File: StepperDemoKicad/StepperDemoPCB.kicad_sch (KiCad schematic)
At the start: 38 parts, among them J1 Conn_01x05_Male, J2 Conn_01x01_Male, J3 Screw_Terminal_01x03, J4 Screw_Terminal_01x04, J5 Screw_Terminal_01x04, J6 Conn_01x06_Male, M1 Stepper_Motor_bipolar, SW1 SW_DIP_x01, U1 L297, U2 L298N

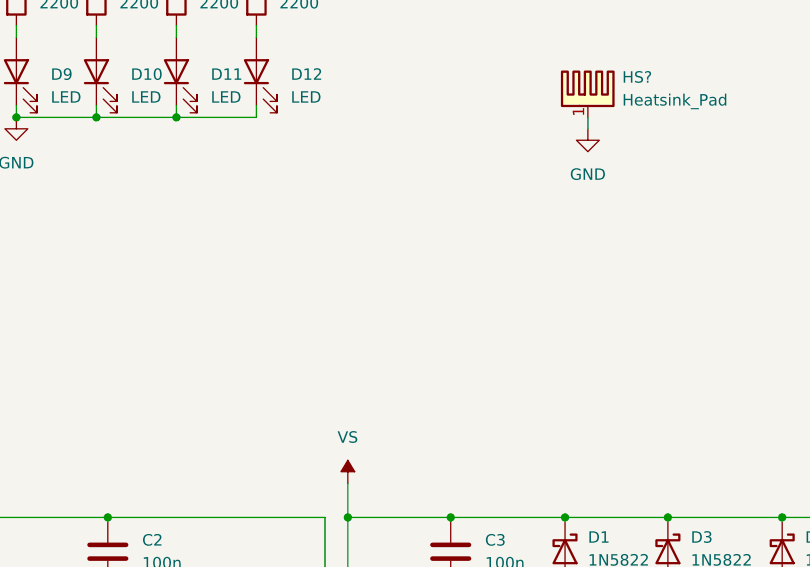
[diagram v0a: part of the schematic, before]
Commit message: smd Diode
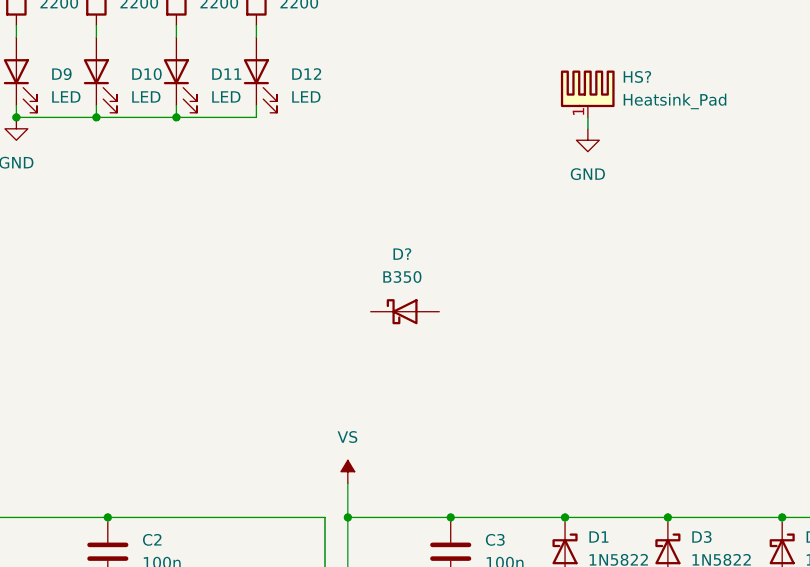
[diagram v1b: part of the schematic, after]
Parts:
- added D?: B350, Diode_SMD:D_SMC, symbol Diode:B350
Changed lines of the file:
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@@
+    (pin "2")
+  )
+  (symbol (lib_id "Diode:B350") (at 156.21 60.96 0) (unit 1)
+    (in_bom yes) (on_board yes) (fields_autoplaced)
+    (property "Reference" "D?" (id 0) (at 155.8925 54.61 0))
+    (property "Value" "B350" (id 1) (at 155.8925 57.15 0))
+    (property "Footprint" "Diode_SMD:D_SMC" (id 2) (at 156.21 65.405 0)
+      (effects (font (size 1.27 1.27)) hide)
+    )
+    (property "Datasheet" "http://www.jameco.com/Jameco/Products/ProdDS/1538777.pdf" (id 3) (at 156.21 60.96 0)
+      (effects (font (size 1.27 1.27)) hide)
+    )
+    (pin "1")
     (pin "2")
   )
@@
       (reference "D12") (unit 1) (value "LED") (footprint "LED_THT:LED_D5.0mm")
     )
+    (path "/86d960eb-ec6c-40c5-9c0c-91477f3b086b"
+      (reference "D?") (unit 1) (value "B350") (footprint "Diode_SMD:D_SMC")
+    )
     (path "/8f6c466e-00c5-43cf-a705-df7cb0e79ac0"

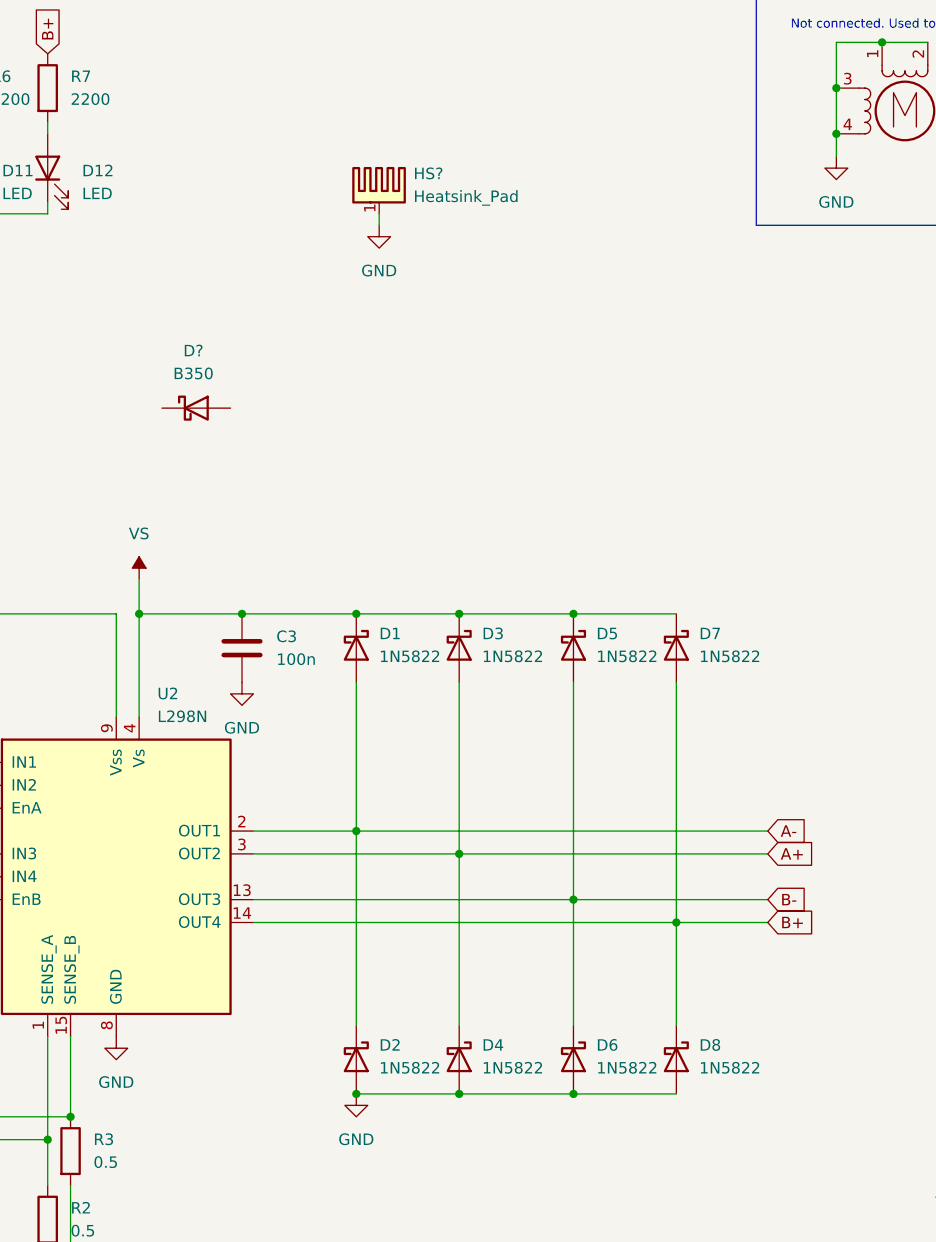
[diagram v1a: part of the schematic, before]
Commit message: Added heatsink
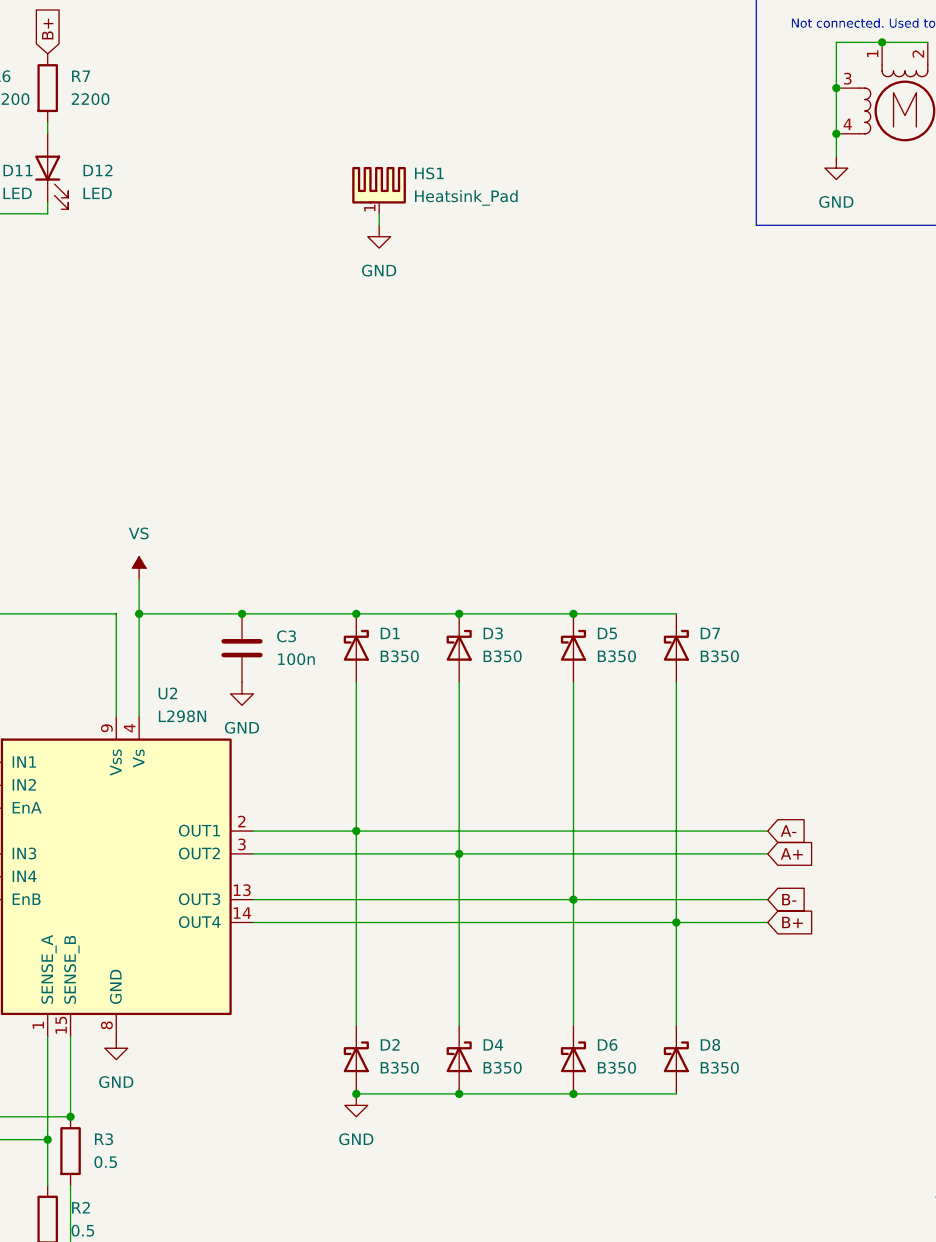
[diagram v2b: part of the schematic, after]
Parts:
- removed D1, D2, D3, D4, D5, D6, D7, D8: 1N5822, Diode_THT:D_DO-201AD_P15.24mm_Horizontal, symbol Diode:1N5822
- added D2, D3, D4, D5, D6, D7, D8: B350, Diode_SMD:D_SMC, symbol Diode:B350
- HS1: renamed from HS?; footprint (none) -> Stepper:42x25mm_multiwatt15
- gave numbers to parts that had none: 1
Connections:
- net A+: now also D3.2 (A), D4.1 (K)
- net A-: now also D1.2 (A), D2.1 (K)
- net B+: now also D7.2 (A), D8.1 (K)
- net B-: now also D5.2 (A), D6.1 (K)
- net GND: now also D2.2 (A), D4.2 (A), D6.2 (A), D8.2 (A)
- net VS: now also D1.1 (K), D3.1 (K), D5.1 (K), D7.1 (K)
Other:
- moved on the sheet: D1

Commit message: SMD resistors
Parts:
- added R? (x6): 2, Resistor_SMD:R_2512_6332Metric_Pad1.40x3.35mm_HandSolder, symbol Device:R
- C1, C2, C3: footprint Resistor_THT:R_Axial_DIN0204_L3.6mm_D1.6mm_P5.08mm_Vertical -> Capacitor_SMD:C_0805_2012Metric_Pad1.18x1.45mm_HandSolder
- R1, R8: footprint Resistor_THT:R_Axial_DIN0204_L3.6mm_D1.6mm_P5.08mm_Vertical -> Resistor_SMD:R_0805_2012Metric_Pad1.20x1.40mm_HandSolder
- R2, R3: value 0.5 -> 2; footprint Resistor_THT:R_Axial_DIN0204_L3.6mm_D1.6mm_P5.08mm_Vertical -> Resistor_SMD:R_2512_6332Metric_Pad1.40x3.35mm_HandSolder
- R4, R5, R6, R7: value 2200 -> 330; footprint Resistor_THT:R_Box_L8.4mm_W2.5mm_P5.08mm -> Resistor_SMD:R_0805_2012Metric_Pad1.20x1.40mm_HandSolder
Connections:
- net A+: no longer R5.1
- net A-: no longer R4.1
- net B+: no longer R7.1
- net B-: no longer R6.1
- net GND: now also R?.2, R?.2, R?.2, R?.2, R?.2, R?.2
- net SensA: now also R?.1, R?.1, R?.1
- net SensB: now also R?.1, R?.1, R?.1
- net SigA+: now also R5.1
- net SigA-: now also R4.1
- net SigB+: now also R7.1
- net SigB-: now also R6.1
